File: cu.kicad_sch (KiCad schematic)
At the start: 8 parts, among them U140 74LS161

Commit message: feat: finished cl
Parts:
- added U143: 74HC02, symbol 74xx:74HC02
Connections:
- net #END_INSTRUCTION: now reaches EEPROM4.19 (I/O7), U140.9 (~{PE})
- net CU1: no longer names the net of EEPROM4.18 (I/O6)
- net CU1: now also U143.2
- net SUPERVISOR_MODE: no longer names the net of EEPROM2.9 (A1), EEPROM3.9 (A1), EEPROM4.9 (A1)
- net SUPERVISOR_MODE: now also U143.1, U143.5
- new net: U143.3, U143.4
- new net ENTER_SUPERVISOR: U143.6
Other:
- note added: "#END_INSTRUCTION"
- note added: "Q"
- note added: "QUIT_SUPERVISOR"
- note added: "RESET"
- note added: "SET"
- note added: "SUPERVISOR_MODE_LATCH"
- note removed: "#CLEAR"

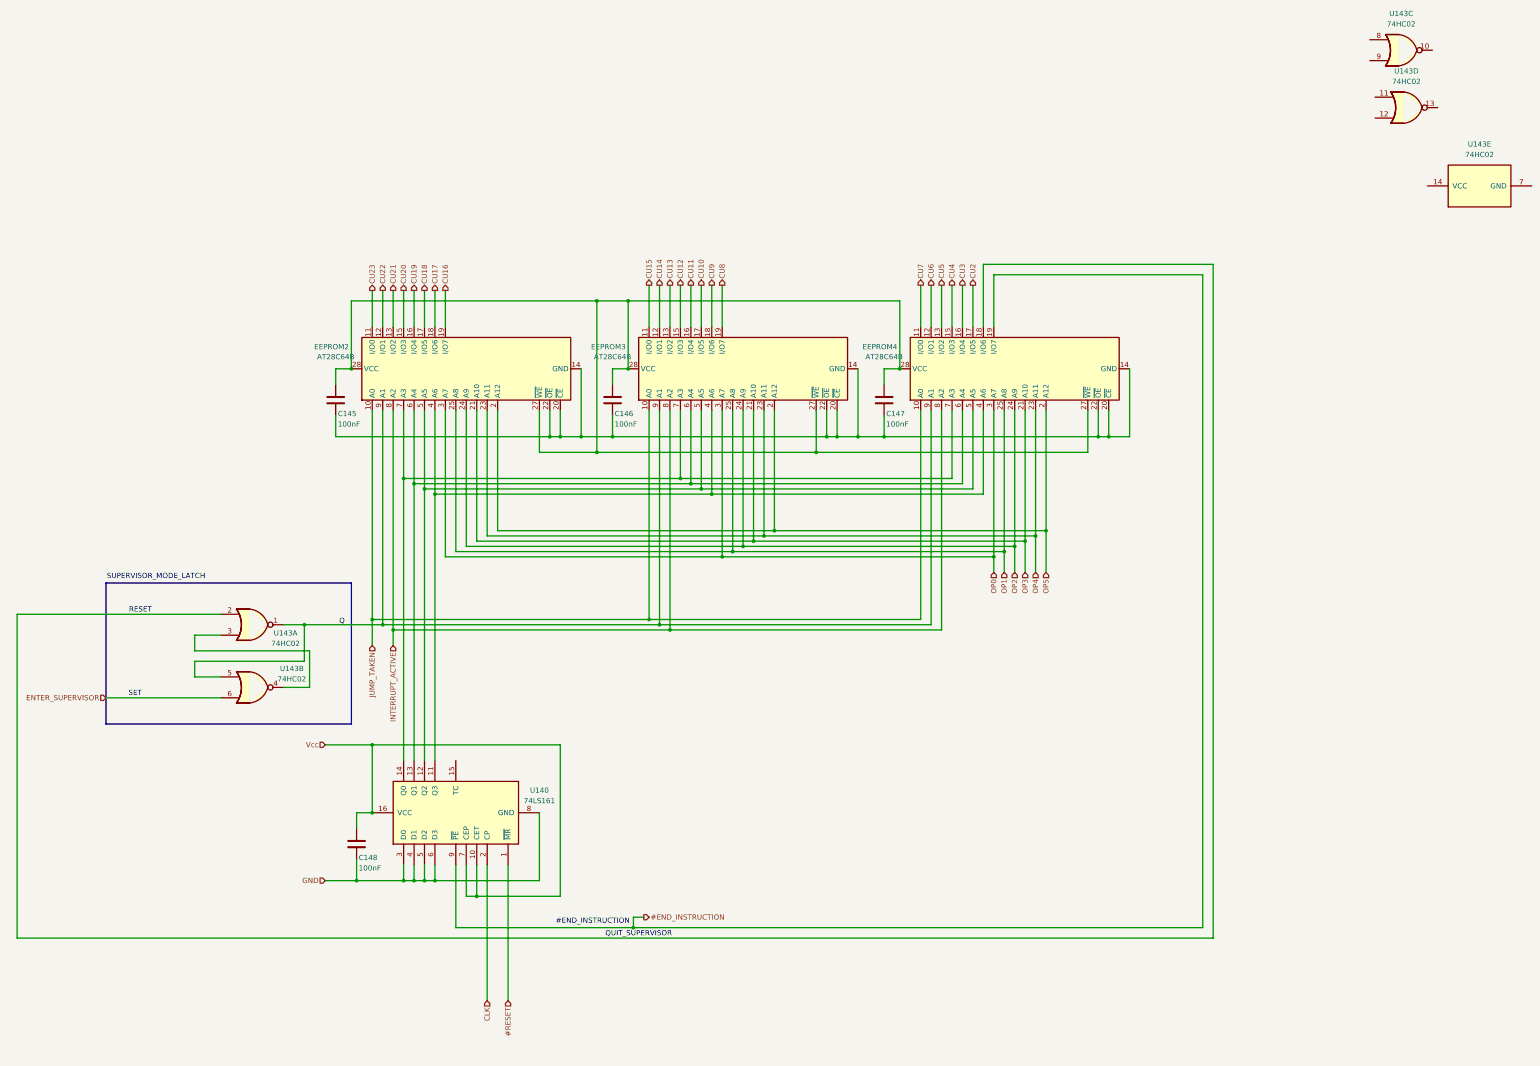
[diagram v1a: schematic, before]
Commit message: feat: connected all control signals to cu
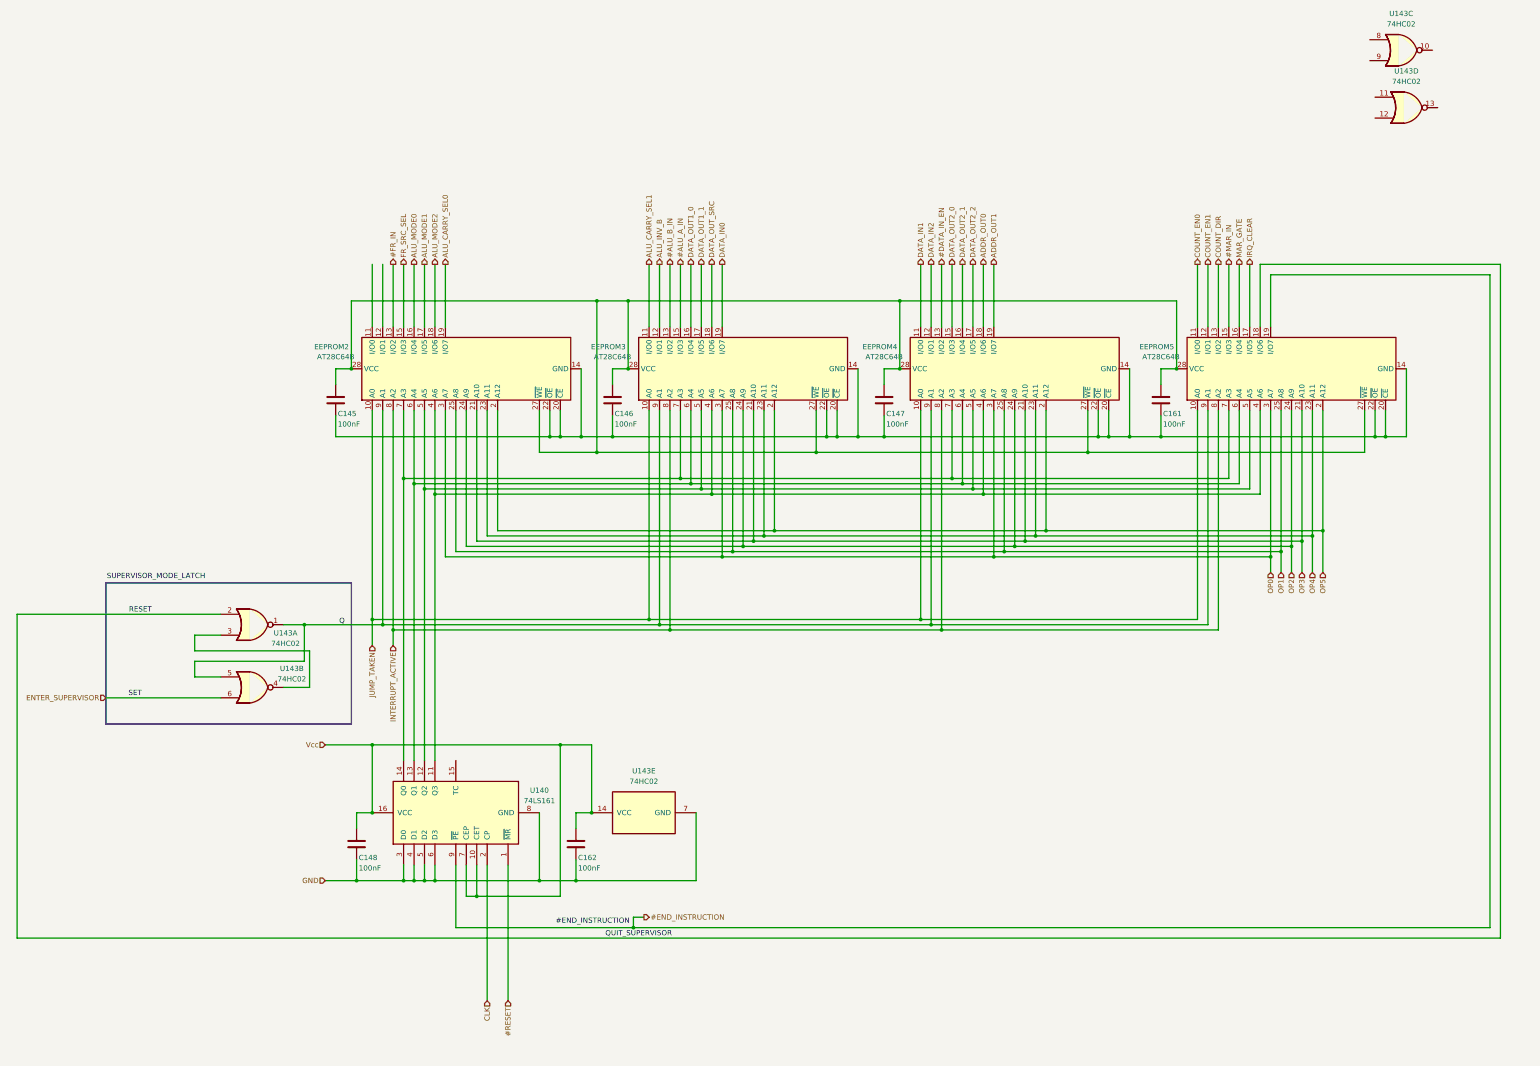
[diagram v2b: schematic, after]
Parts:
- added C161, C162: 100nF, Capacitor_THT:C_Disc_D3.0mm_W1.6mm_P2.50mm, symbol Device:C
- added EEPROM5: AT28C64B, Package_DIP:DIP-28_W15.24mm, symbol Memory_EEPROM:KM28C64A
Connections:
- net #END_INSTRUCTION: now also EEPROM5.19 (I/O7); no longer EEPROM4.19 (I/O7)
- net GND: now also U143.7 (GND), C162.2
- net INTERRUPT_ACTIVE: now also EEPROM5.8 (A2)
- net JUMP_TAKEN: now also EEPROM5.10 (A0)
- net OP0: now also EEPROM5.3 (A7)
- net OP1: now also EEPROM5.25 (A8)
- net OP2: now also EEPROM5.24 (A9)
- net OP3: now also EEPROM5.21 (A10)
- net OP4: now also EEPROM5.23 (A11)
- net OP5: now also EEPROM5.2 (A12)
- net Vcc: now also U143.14 (VCC), C162.1
- net at C145.2, C146.2, C147.2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: now also C161.2, EEPROM5.14 (GND), EEPROM5.20 (~{CE}), EEPROM5.22 (~{OE})
- net at U143.2: now also EEPROM5.18 (I/O6); no longer EEPROM4.18 (I/O6)
- net at C145.1, C146.1, C147.1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: now also C161.1, EEPROM5.27 (~{WE}), EEPROM5.28 (VCC)
- net at EEPROM2.4 (A6), EEPROM3.4 (A6), EEPROM4.4 (A6)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: now also EEPROM5.4 (A6)
- net at EEPROM2.5 (A5), EEPROM3.5 (A5), EEPROM4.5 (A5)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: now also EEPROM5.5 (A5)
- net at EEPROM2.6 (A4), EEPROM3.6 (A4), EEPROM4.6 (A4)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: now also EEPROM5.6 (A4)
- net at EEPROM2.7 (A3), EEPROM3.7 (A3), EEPROM4.7 (A3)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: now also EEPROM5.7 (A3)
- net at EEPROM2.9 (A1), EEPROM3.9 (A1), EEPROM4.9 (A1)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: now also EEPROM5.9 (A1)
- net CU10 renamed DATA_OUT1_1
- net CU11 renamed DATA_OUT1_0
- net CU12 renamed #ALU_A_IN
- net CU13 renamed #ALU_B_IN
- net CU14 renamed ALU_INV_B
- net CU15 renamed ALU_CARRY_SEL1
- net CU16 renamed ALU_CARRY_SEL0
- net CU17 renamed ALU_MODE2
- net CU18 renamed ALU_MODE1
- net CU19 renamed ALU_MODE0
- net CU2 renamed DATA_OUT2_2
- net CU20 renamed FR_SRC_SEL
- net CU21 renamed #FR_IN
- net CU22: no longer names the net of EEPROM2.12 (I/O1)
- net CU23: no longer names the net of EEPROM2.11 (I/O0)
- net CU3 renamed DATA_OUT2_1
- net CU4 renamed DATA_OUT2_0
- net CU5 renamed #DATA_IN_EN
- net CU6 renamed DATA_IN2
- net CU7 renamed DATA_IN1
- net CU8 renamed DATA_IN0
- net CU9 renamed DATA_OUT_SRC
- new net #MAR_IN: EEPROM5.15 (I/O3)
- new net ADDR_OUT0: EEPROM4.18 (I/O6)
- new net ADDR_OUT1: EEPROM4.19 (I/O7)
- new net COUNT_DIR: EEPROM5.13 (I/O2)
- new net COUNT_EN0: EEPROM5.11 (I/O0)
- new net COUNT_EN1: EEPROM5.12 (I/O1)
- new net IRQ_CLEAR: EEPROM5.17 (I/O5)
- new net MAR_GATE: EEPROM5.16 (I/O4)
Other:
- moved on the sheet: U143E

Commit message: feat: created and connected all functional components
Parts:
- added C163: 100nF, Capacitor_THT:C_Disc_D3.0mm_W1.6mm_P2.50mm, symbol Device:C
- added U151: 74HC00, Connector_RJ:RJ45_HALO_HFJ11-x2450E-LxxRL_Horizontal, symbol 74xx:74HC00
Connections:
- net ENTER_SUPERVISOR is gone; now on an unnamed net: U143.6
- net GND: now also C163.2, U151.7 (GND)
- net Vcc: now also C163.1, U151.14 (VCC)
- net #END_INSTRUCTION: no longer names the net of EEPROM5.19 (I/O7), U140.9 (~{PE})
- net #END_INSTRUCTION: now also U151.1, U151.2
- net INTERRUPT_ACTIVE: no longer names the net of EEPROM2.8 (A2), EEPROM3.8 (A2), EEPROM4.8 (A2), EEPROM5.8 (A2)
- net INTERRUPT_ACTIVE: now also U151.8
- new net: U151.3, U151.4
- new net: U151.10, U151.6, U151.9
- new net IRQ: U151.5
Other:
- note added: "INTERRUPT_ACTIVE"
- note added: "NOT((IRQ) NAND (NOT(#END_INSTRUCTION))) IRQ AND END_INSTRUCTION"
- note added: "UNUSED LOGIC GATES"
- moved on the sheet: U143C, U143D

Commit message: feat: created RESET signal
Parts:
- added C165, C166: 100nF, Capacitor_THT:C_Disc_D3.0mm_W1.6mm_P2.50mm, symbol Device:C
- added U154: 74HC02, symbol 74xx:74HC02
- added U155: 74LS08, symbol 74xx:74LS08
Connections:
- net Vcc is gone; now on net +5V: C148.1, C162.1, C163.1, U140.10 (CET), U140.16 (VCC), U140.7 (CEP), U143.14 (VCC), U151.14 (VCC)
- net #RESET: now also U143.11, U143.12, U154.11, U154.12
- net GND: now also C145.2, C146.2, C147.2, C161.2, EEPROM2.14 (GND), EEPROM2.20 (~{CE}), EEPROM2.22 (~{OE}), EEPROM3.14 (GND), EEPROM3.20 (~{CE}), EEPROM3.22 (~{OE}), EEPROM4.14 (GND), EEPROM4.20 (~{CE}), EEPROM4.22 (~{OE}), EEPROM5.14 (GND), EEPROM5.20 (~{CE}), EEPROM5.22 (~{OE}), C165.2, C166.2, U155.7 (GND)
- net at U151.11: now also U143.6
- net at U151.12: now also U143.10, U151.13
- net +5V: now reaches C145.1, C146.1, C147.1, C161.1, EEPROM2.27 (~{WE}), EEPROM2.28 (VCC), EEPROM3.27 (~{WE}), EEPROM3.28 (VCC), EEPROM4.27 (~{WE}), EEPROM4.28 (VCC), EEPROM5.27 (~{WE}), EEPROM5.28 (VCC)
- net +5V: now also C165.1, C166.1, U154.14 (VCC), U155.14 (VCC)
- net at EEPROM2.8 (A2), EEPROM3.8 (A2), EEPROM4.8 (A2)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: now also U155.11; no longer U151.8
- net at U143.8: now also EEPROM2.11 (I/O0)
- net at U143.9: now also U143.13
- net at EEPROM2.12 (I/O1): now also U154.6
- new net: U154.1, U154.5, U155.13
- new net: U154.13, U154.2
- new net: U154.3, U154.4
- new net: U151.8, U155.12
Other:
- note added: "CPU_MODE_LATCH 0: BOOT 1: NORMAL OPERATION"
- note added: "NOT from one NOR"
- note added: "OR from NAND and NOR"
- note removed: "UNUSED LOGIC GATES"
- moved on the sheet: U143C, U143D, U151D
